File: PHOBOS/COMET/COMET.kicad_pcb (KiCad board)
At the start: 4 copper layers, 63.5 x 25.4 mm, 72 parts, among them J1 USB4056-03-A_REVA2, J2 M/D, J5 Power/Arm, Q1 SiSS63DN, Q2 PMGD175XNEX, Q3 SiSS63DN, SW1 SW_SPDT, SW3 KMR211GLFS, U1 MPL3115A2, U2 LSM6DS3, U3 W25Q128JVSIQ, U4 NCP1117-3.3_SOT223, U5 RP2040, Y1 ABM8-272-T3

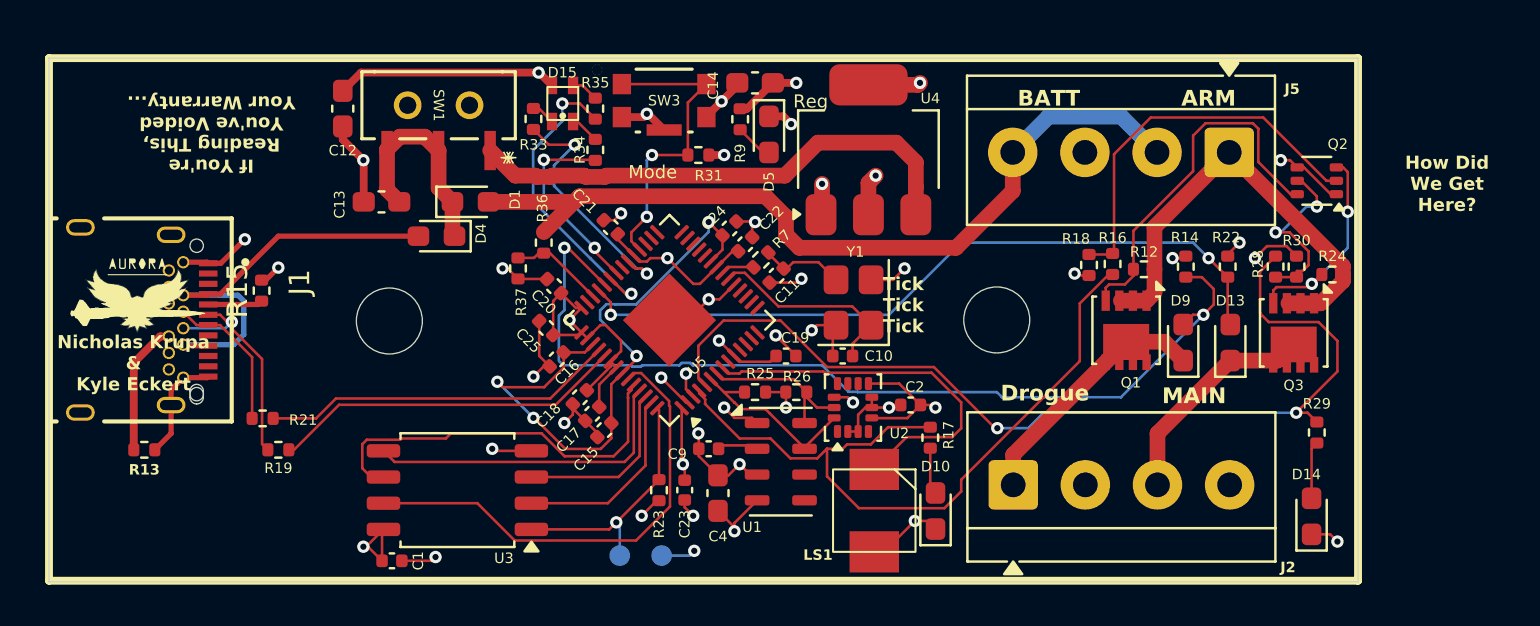
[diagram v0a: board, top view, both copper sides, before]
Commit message: Comet files reset. Mounting holes are currently centered.
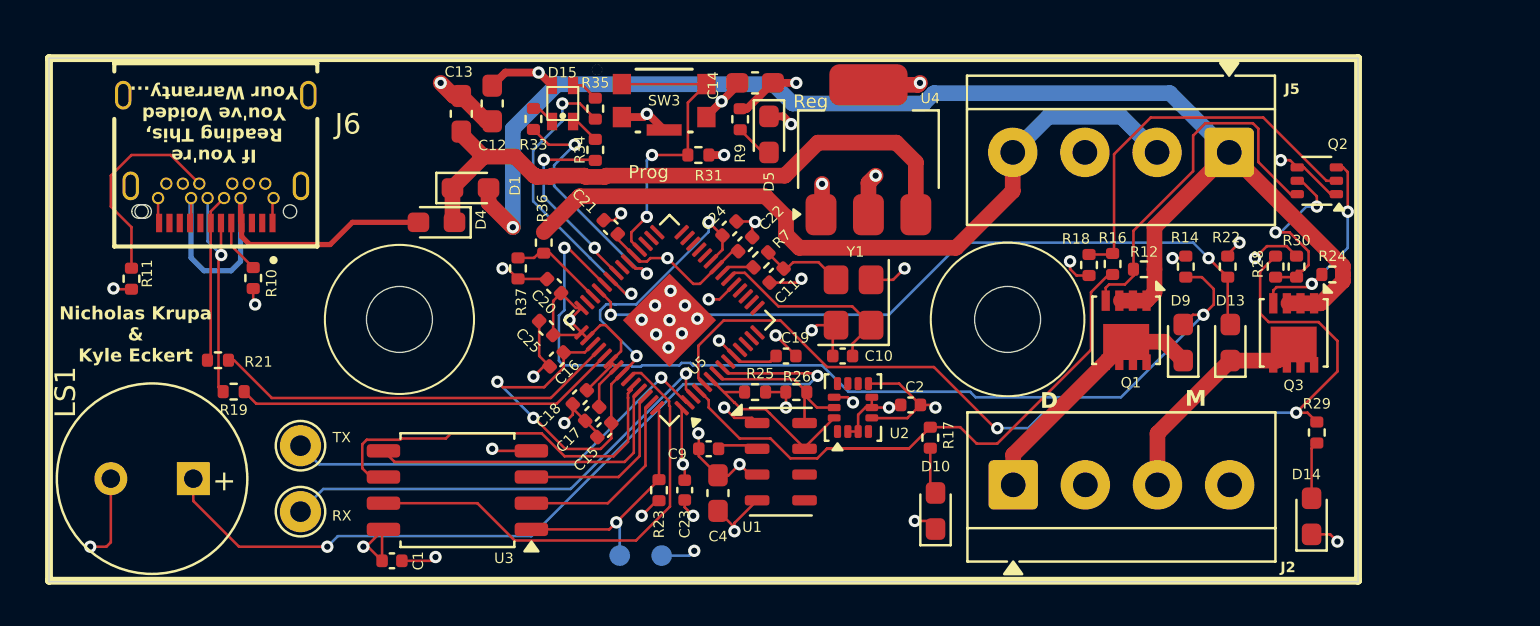
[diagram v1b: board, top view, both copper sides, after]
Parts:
- removed J1: USB4056-03-A_REVA2, USB4056-03-A:GCT_USB4056-03-A_REVA2
- removed R13, R15: 5.1k, Resistor_SMD:R_0402_1005Metric
- removed SW1: SW_SPDT, External/Custom Parts:SWITCH_102AGRLC
- added J6: USB4056-03-A_REVA2, USB4056-03-A:GCT_USB4056-03-A_REVA2, F.Cu at (75.4, 62.7)
- added R10: 5.1k, Resistor_SMD:R_0402_1005Metric, F.Cu at (77.2, 71.5)
- added R11: 5.1k, Resistor_SMD:R_0402_1005Metric, F.Cu at (71.3, 71.6)
- added TP3: TX, TestPoint:TestPoint_THTPad_D2.0mm_Drill1.0mm, F.Cu at (79.5, 79.7)
- added TP4: RX, TestPoint:TestPoint_THTPad_D2.0mm_Drill1.0mm, F.Cu at (79.5, 82.9)
- LS1: footprint External/Custom Parts:OWMB-404020SA-40-17 -> Buzzer_Beeper:MagneticBuzzer_PUI_AT-0927-TT-6-R
- Q1, Q3: value SiSS63DN -> SISS67DN-T1-GE3
- Q2: value PMGD175XNEX -> BSD840N
- moved LS1 29.7 mm to (74.3, 81.3), turned to 180 degrees
- moved C12 7.25 mm to (88.8, 63.1)
- moved C13 5.77 mm to (87.3, 63.6), turned to 90 degrees
- moved R19 3.56 mm to (76.2, 77.0)
- moved R21 3.56 mm to (75.5, 75.5)
- moved D1 0.67 mm to (87.7, 67.2)
- moved D4 0.67 mm to (86.1, 68.8)
- moved H1 0.53 mm to (113.8, 73.5)
- moved H2 0.50 mm to (84.3, 73.5)
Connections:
- C13 pad 1: VIN -> V+
- D1 pad 1: VIN -> V+
- D1 pad 2: +BATT -> VMOS
- D4 pad 1: VIN -> V+
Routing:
- net VMOS: track 21.7 -> 66.4 mm, vias 0 -> 1
- net /Speaker: track 18.7 -> 40.5 mm, vias 0 -> 2
- net /RX: track 1.26 -> 22.8 mm
- net /TX: track 1.77 -> 21.9 mm
- net Net-(J6-CC2): track 0.00 -> 10.5 mm
- net VIN: track 10.3 -> 0.00 mm
- net +3V3: track 70.0 -> 62.7 mm
- net GND: track 71.4 -> 64.9 mm, vias 29 -> 39
- net Net-(J1-CC2): track 6.45 -> 0.00 mm
- net V+: track 24.9 -> 30.6 mm
- net /MOS_M: track 35.9 -> 31.6 mm
- net +BATT: track 40.6 -> 36.5 mm
- net Net-(J1-CC1): track 2.66 -> 0.00 mm
- net Net-(J6-CC1): track 0.00 -> 2.60 mm
- net /USB_-: track 17.2 -> 19.7 mm
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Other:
- board text added: "D"
- board text added: "DROGUE"
- board text added: "M"
- board text added: "Prog"
- board text added: "RX"
- board text added: "SWITCH"
- board text added: "TX"
- board text removed: "ARM"
- board text removed: "C.O.M.E.T."
- board text removed: "Compact Onboard Management for Ejection Timing"
- board text removed: "Drogue"
- board text removed: "Fish Approved"
- board text removed: "How Did We Get Here?"
- board text removed: "Mode"
- board text removed: "Rx"
- board text removed: "Swimming Pool"
- board text removed: "Tick Tick Tick"
- board text removed: "Tx"
- board text removed: "{dblquote}Is he playing Monopoly{dblquote} Jolene"

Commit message: unrouted, relocated, centering ensured. Dimensions added.
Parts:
- moved LS1 17.4 mm to (82.5, 65.9)
- moved J6 12.7 mm to (68.8, 73.6), turned to -90 degrees
- moved R11 8.82 mm to (77.7, 77.6), turned to 180 degrees
- moved R19 2.26 mm to (78.4, 76.6)
- moved R21 2.26 mm to (77.7, 75.1)
- moved R10 0.52 mm to (77.7, 71.7), turned to 0 degrees
- moved D4 0.51 mm to (86.6, 68.8)
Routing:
- net VMOS: track 66.4 -> 0.00 mm, vias 1 -> 0
- net GND: track 64.9 -> 0.00 mm, vias 39 -> 0
- net +3V3: track 62.7 -> 0.00 mm, vias 18 -> 0
- net /MOS_D: track 46.9 -> 0.00 mm, vias 2 -> 0
- net /MAIN_CONT: track 46.3 -> 0.00 mm, vias 2 -> 0
- net /Speaker: track 40.5 -> 0.00 mm, vias 2 -> 0
- net +BATT: track 36.5 -> 0.00 mm
- net /DROGUE_CONT: track 35.8 -> 0.00 mm, vias 2 -> 0
- net /MOS_M: track 31.6 -> 0.00 mm
- net V+: track 30.6 -> 0.00 mm
- net +1V1: track 30.3 -> 0.00 mm, vias 4 -> 0
- net /QSPI_SD3: track 23.1 -> 0.00 mm
- net /RX: track 22.8 -> 0.00 mm, vias 1 -> 0
- net /TX: track 21.9 -> 0.00 mm, vias 1 -> 0
- net VBUS: track 21.1 -> 0.00 mm
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
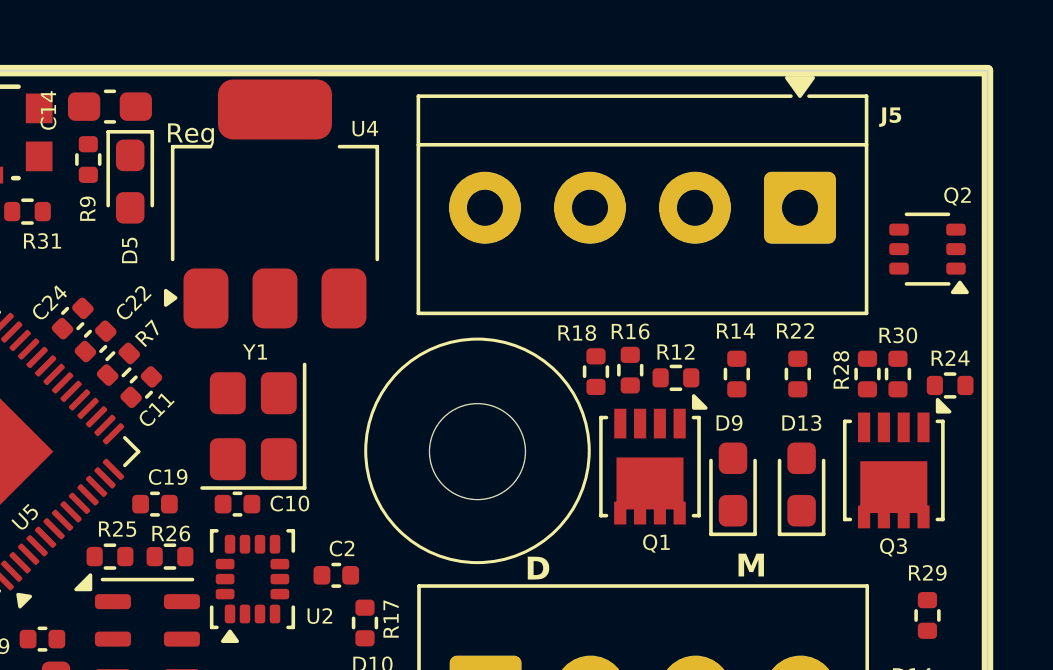
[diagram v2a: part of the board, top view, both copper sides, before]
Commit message: Arming is back. VMOS now does not break power to board
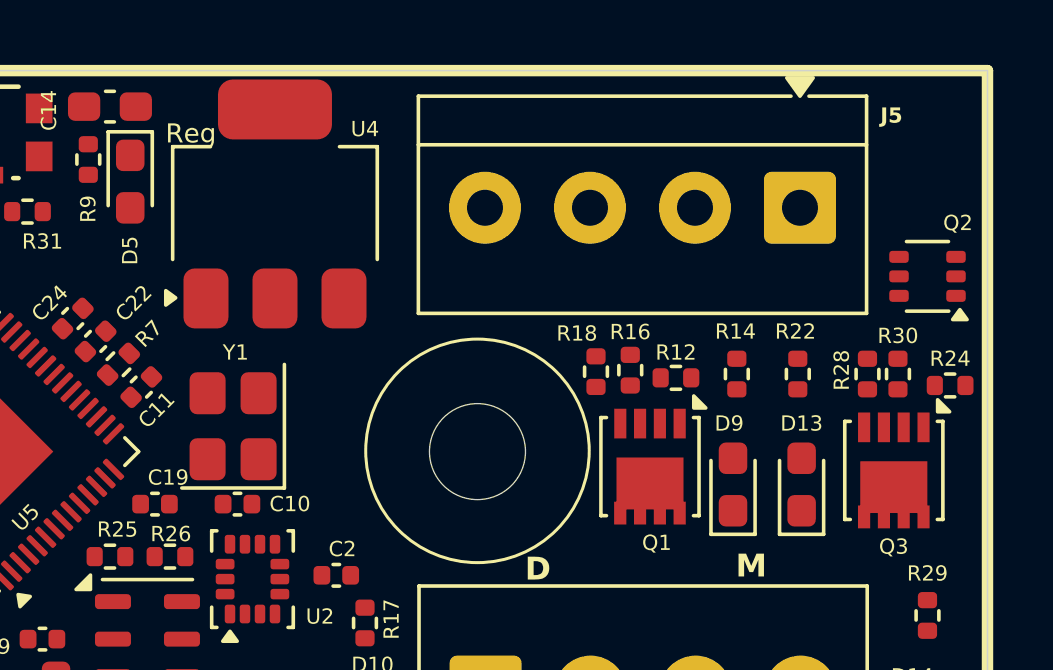
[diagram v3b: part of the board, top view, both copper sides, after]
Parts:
- moved Q2 0.91 mm to (128.8, 67.7)
- moved Y1 0.67 mm to (105.6, 72.7)
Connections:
- D1 pad 2: VMOS -> +BATT

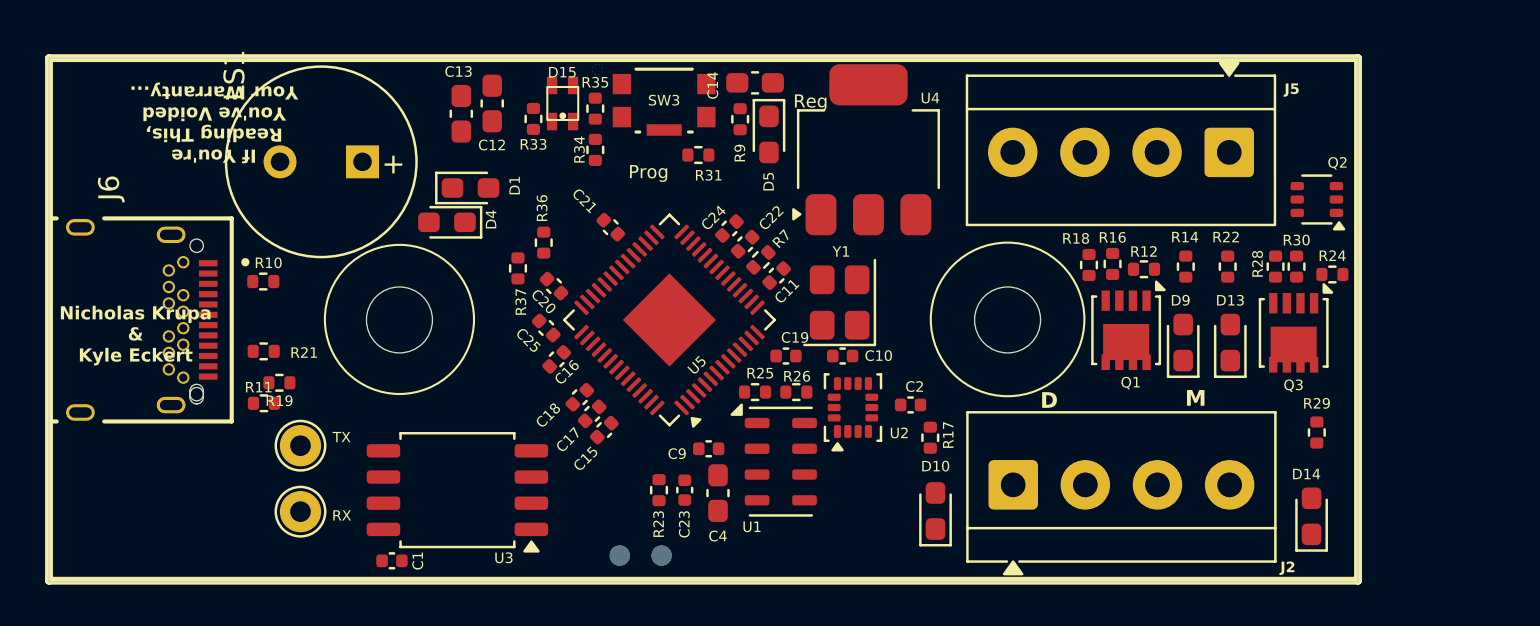
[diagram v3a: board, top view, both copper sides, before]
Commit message: Board re-routed. NMos moved in.
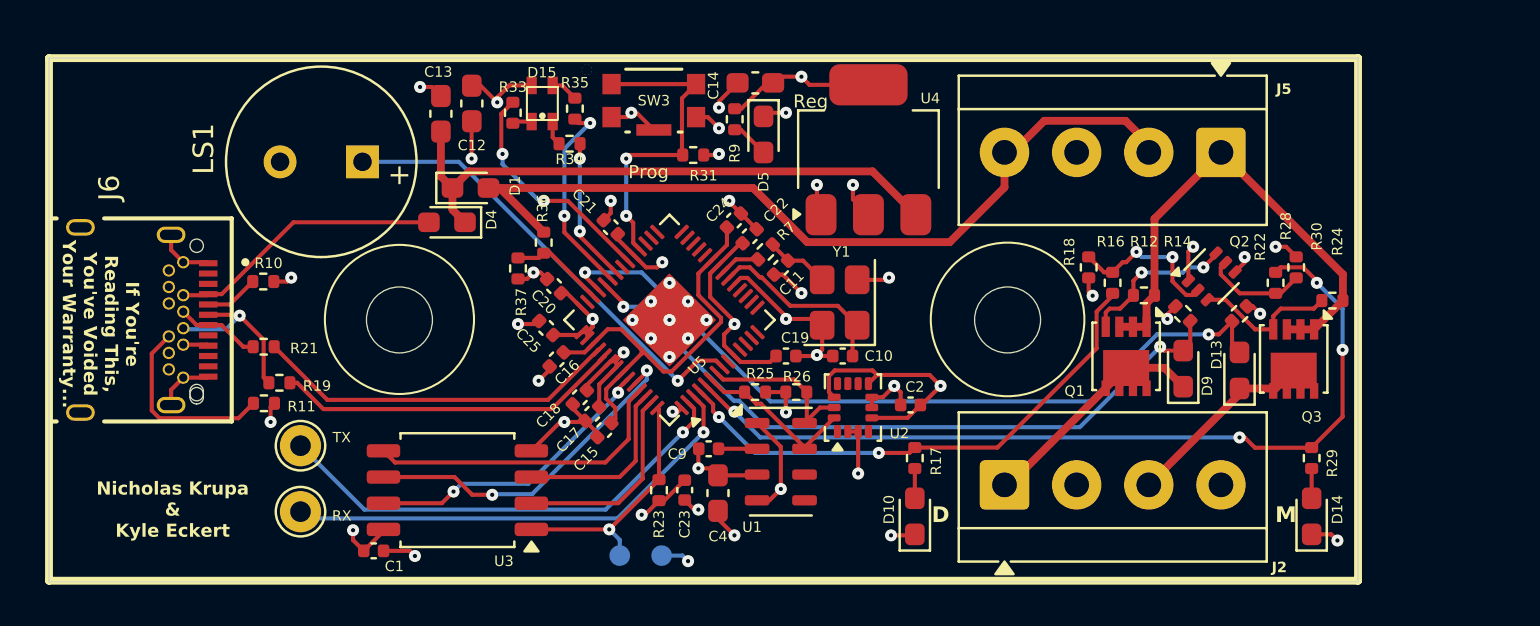
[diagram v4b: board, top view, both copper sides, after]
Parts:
- moved Q2 6.32 mm to (123.7, 71.4), turned to 45 degrees
- moved R22 2.36 mm to (125.0, 73.3), turned to 45 degrees
- moved R14 2.29 mm to (122.3, 73.3), turned to -45 degrees
- moved D13 1.42 mm to (125.0, 76.0)
- moved R34 1.29 mm to (92.5, 65.0), turned to 0 degrees
- moved D9 1.27 mm to (122.3, 75.9)
- moved Q3 1.27 mm to (127.6, 75.5)
- moved R12 1.27 mm to (120.4, 72.4)
- moved R24 1.27 mm to (129.5, 72.6)
- moved Q1 1.27 mm to (119.5, 75.3)
- moved R29 1.26 mm to (128.5, 80.3)
- moved R17 1.24 mm to (109.3, 80.3)
- moved R33 1.04 mm to (89.8, 63.5), turned to 90 degrees
- moved D10 1.04 mm to (109.3, 83.1)
- moved C1 1.01 mm to (83.0, 84.8)
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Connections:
- net V+ renamed VIN
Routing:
- net +3V3: track 0.00 -> 64.5 mm, vias 0 -> 17
- net GND: track 0.00 -> 63.3 mm, vias 0 -> 40
- net /MOS_D: track 0.00 -> 42.3 mm, vias 0 -> 4
- net +BATT: track 0.00 -> 40.7 mm
- net /DROGUE_CONT: track 0.00 -> 38.4 mm, vias 0 -> 2
- net /MAIN_CONT: track 0.00 -> 34.3 mm, vias 0 -> 2
- net VIN: track 0.00 -> 28.6 mm
- net /MOS_M: track 0.00 -> 25.8 mm, vias 0 -> 2
- net VMOS: track 0.00 -> 24.2 mm
- net /RX: track 0.00 -> 23.4 mm, vias 0 -> 1
- net /TX: track 0.00 -> 23.2 mm, vias 0 -> 1
- net /Speaker: track 0.00 -> 22.4 mm, vias 0 -> 1
- net +1V1: track 0.00 -> 20.1 mm
- net /USB_-: track 0.00 -> 17.8 mm
- net /USB_+: track 0.00 -> 16.9 mm
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- added copper zone on In2.Cu, net VBUS

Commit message: 3d Models added back into parts folder
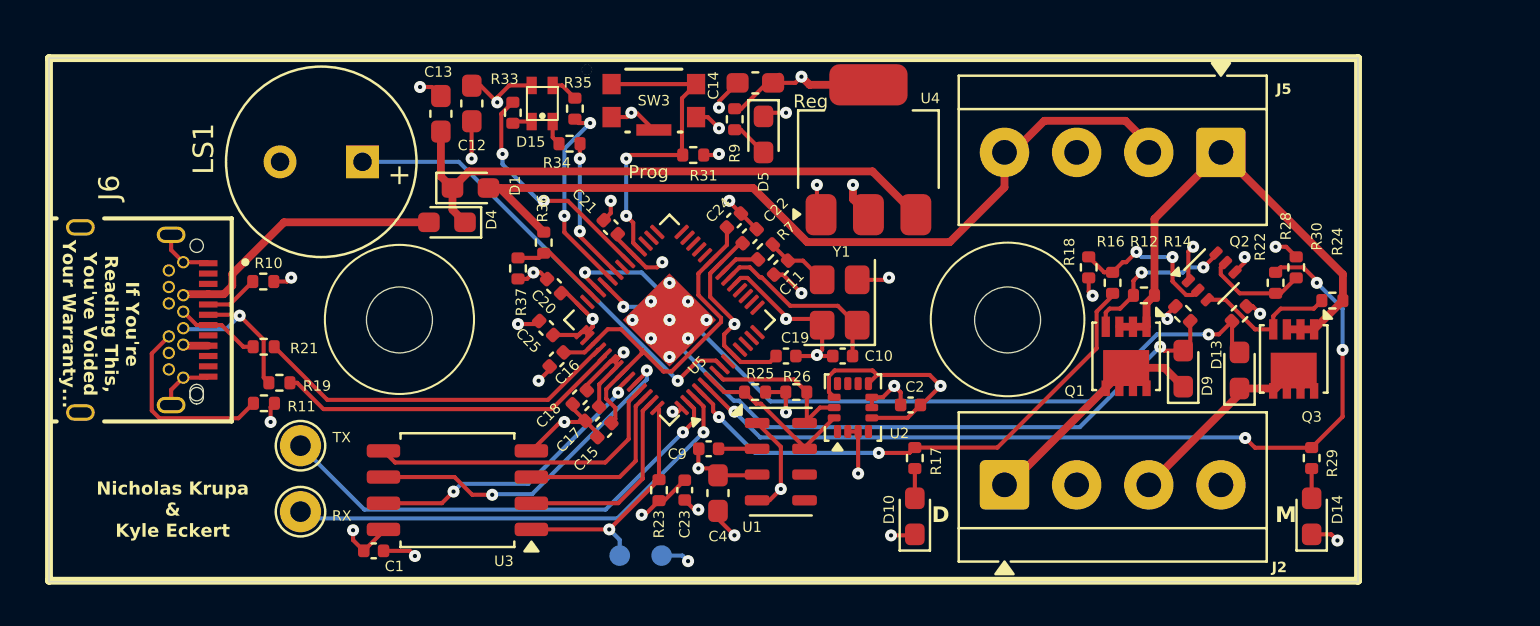
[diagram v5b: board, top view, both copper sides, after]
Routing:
- added copper zone on In2.Cu, net +3V3
- added copper zone on In1.Cu, net GND
- removed copper zone on In1.Cu, net +3V3
- removed copper zone on In2.Cu, net GND
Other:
- board text added: "- BATT +"
- board text added: "ARM"
- board text removed: "BATT"
- board text removed: "SWITCH"
